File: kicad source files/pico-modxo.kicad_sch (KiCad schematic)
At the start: 9 parts, among them J1 XBOX_LPC, U1 Pico

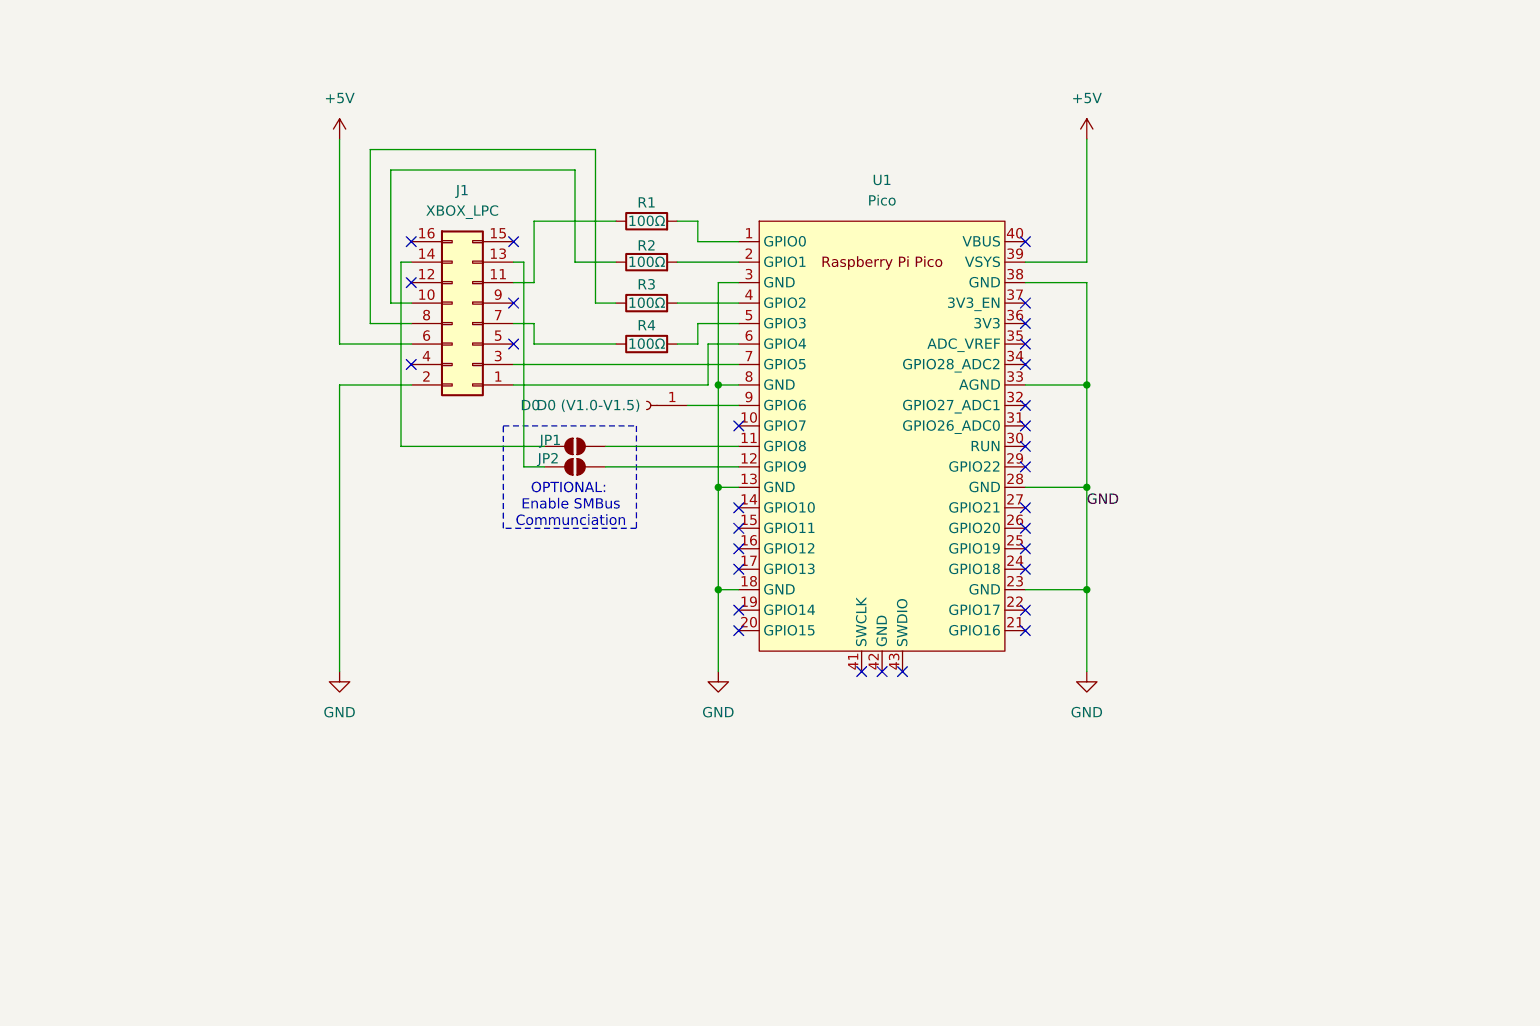
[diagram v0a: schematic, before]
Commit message: V2 Design
V2 Design based on EqUiNoX schematic 1.0 2024-07-29
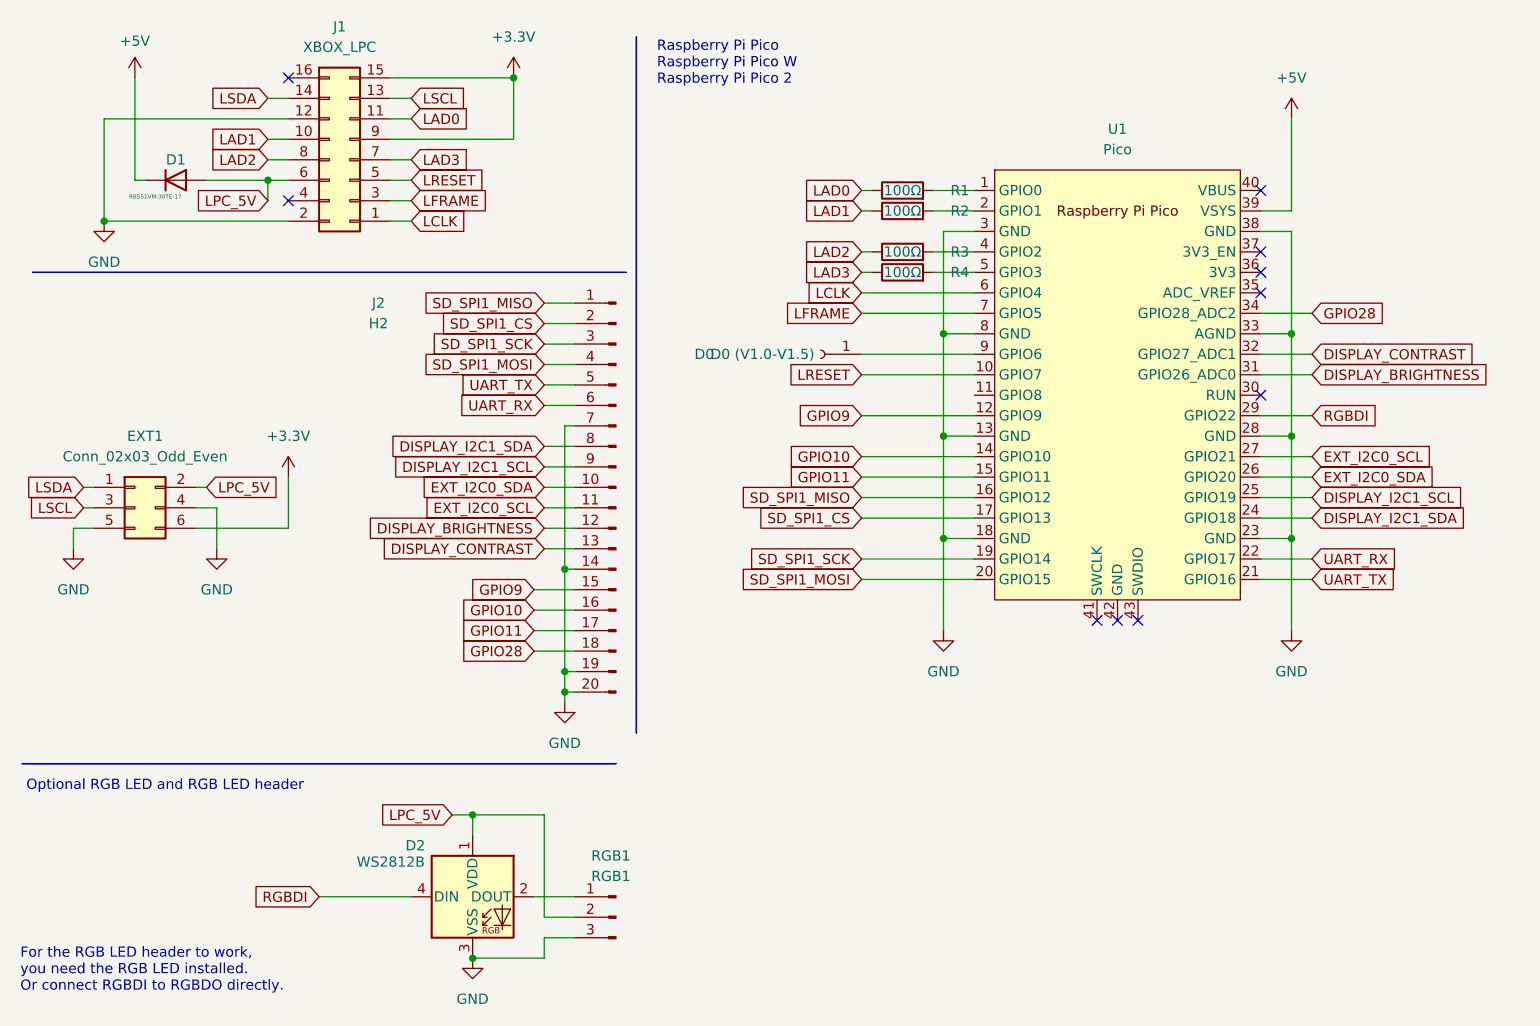
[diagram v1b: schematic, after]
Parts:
- removed JP1, JP2: SolderJumper_2_Open, Jumper:SolderJumper-2_P1.3mm_Open_RoundedPad1.0x1.5mm, symbol Jumper:SolderJumper_2_Open
- added D1: RB551VM-30TE-17, Diode_SMD:D_MELF-RM10_Universal_Handsoldering, symbol Device:D
- added D2: WS2812B, LED_SMD:LED_WS2812B_PLCC4_5.0x5.0mm_P3.2mm, symbol LED:WS2812B
- added EXT1: Conn_02x03_Odd_Even, Connector_PinHeader_2.54mm:PinHeader_2x03_P2.54mm_Vertical, symbol Connector_Generic:Conn_02x03_Odd_Even
- added J2: H2, Connector_Molex:Molex_SL_171971-0020_1x20_P2.54mm_Vertical, symbol Connector:Conn_01x20_Pin
- added RGB1: RGB1, Connector:FanPinHeader_1x03_P2.54mm_Vertical, symbol Connector:Conn_01x03_Pin
- J1: footprint XBOX_LPC:XBOX_LPC -> xbox_lpc:xbox_lpc
- R1, R2, R3, R4: footprint Resistor_THT:R_Axial_DIN0207_L6.3mm_D2.5mm_P7.62mm_Horizontal -> Resistors_Universal:Resistor_SMD+THTuniversal_1206_RM10_HandSoldering
- U1: footprint RPi_Pico:RPi_Pico_SMD_TH -> MCU_RaspberryPi_and_Boards:RPi_Pico_SMD_TH; symbol pico:Pico -> MCU_RaspberryPi_and_Boards:Pico
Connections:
- net +5V: now also D1.1 (K); no longer J1.6 (5V)
- net GND: now also J1.12 (GND), D2.3 (VSS), EXT1.4 (Pin_4), EXT1.5 (Pin_5), J2.14 (Pin_14), J2.19 (Pin_19), J2.20 (Pin_20), J2.7 (Pin_7), RGB1.3 (Pin_3)
- net LAD1: now reaches J1.10 (LAD1), R2.1
- net LAD3: now reaches J1.7 (LAD3), R4.1
- net LAD2: now reaches J1.8 (LAD2), R3.1
- net LSDA: now reaches J1.14 (SDA)
- net LSDA: now also EXT1.1 (Pin_1)
- net LAD0: now reaches J1.11 (LAD0), R1.1
- net LRESET: now reaches U1.10 (GPIO7)
- net LRESET: now also J1.5 (LRESET#)
- net GPIO9: now reaches U1.12 (GPIO9)
- net GPIO9: now also J2.15 (Pin_15)
- net GPIO10: now reaches U1.14 (GPIO10)
- net GPIO10: now also J2.16 (Pin_16)
- net GPIO11: now reaches U1.15 (GPIO11)
- net GPIO11: now also J2.17 (Pin_17)
- net SD_SPI1_MISO: now reaches U1.16 (GPIO12)
- net SD_SPI1_MISO: now also J2.1 (Pin_1)
- net SD_SPI1_CS: now reaches U1.17 (GPIO13)
- net SD_SPI1_CS: now also J2.2 (Pin_2)
- net SD_SPI1_SCK: now reaches U1.19 (GPIO14)
- net SD_SPI1_SCK: now also J2.3 (Pin_3)
- net SD_SPI1_MOSI: now reaches U1.20 (GPIO15)
- net SD_SPI1_MOSI: now also J2.4 (Pin_4)
- net UART_TX: now reaches U1.21 (GPIO16)
- net UART_TX: now also J2.5 (Pin_5)
- net UART_RX: now reaches U1.22 (GPIO17)
- net UART_RX: now also J2.6 (Pin_6)
- net DISPLAY_I2C1_SDA: now reaches U1.24 (GPIO18)
- net DISPLAY_I2C1_SDA: now also J2.8 (Pin_8)
- net DISPLAY_I2C1_SCL: now reaches U1.25 (GPIO19)
- net DISPLAY_I2C1_SCL: now also J2.9 (Pin_9)
- net EXT_I2C0_SDA: now reaches U1.26 (GPIO20)
- net EXT_I2C0_SDA: now also J2.10 (Pin_10)
- net EXT_I2C0_SCL: now reaches U1.27 (GPIO21)
- net EXT_I2C0_SCL: now also J2.11 (Pin_11)
- net RGBDI: now reaches U1.29 (GPIO22)
- net RGBDI: now also D2.4 (DIN)
- net DISPLAY_BRIGHTNESS: now reaches U1.31 (GPIO26_ADC0)
- net DISPLAY_BRIGHTNESS: now also J2.12 (Pin_12)
- net DISPLAY_CONTRAST: now reaches U1.32 (GPIO27_ADC1)
- net DISPLAY_CONTRAST: now also J2.13 (Pin_13)
- net GPIO28: now reaches U1.34 (GPIO28_ADC2)
- net GPIO28: now also J2.18 (Pin_18)
- net LCLK: now reaches J1.1 (LCLK), U1.6 (GPIO4)
- net LFRAME: now reaches J1.3 (LFRAME#), U1.7 (GPIO5)
- net LSCL: now reaches J1.13 (SCL)
- net LSCL: now also EXT1.3 (Pin_3)
- net +3.3V: now reaches J1.15 (3.3V)
- net +3.3V: now also J1.9 (3.3V), EXT1.6 (Pin_6)
- new net: D2.2 (DOUT), RGB1.1 (Pin_1)
- new net LPC_5V: D1.2 (A), D2.1 (VDD), EXT1.2 (Pin_2), J1.6 (5V), RGB1.2 (Pin_2)
- no-connect marks 31 -> 10
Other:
- note added: "Optional RGB LED and RGB LED header"
- note added: "Raspberry Pi Pico Raspberry Pi Pico W Raspberry Pi Pico 2"
- note removed: "Enable SMBus Communciation"
- note removed: "OPTIONAL:"
- company: (none) -> Version for future PrometheOS functionalities
- moved on the sheet: D0, J1, R1, R2, R3, R4, U1

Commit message: Move GND add GP8
added Gp8 connected to 3.3v
moved GND to bottom.
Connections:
- net +3.3V: now also U1.11 (GPIO8)
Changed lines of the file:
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@@
+	(wire
+		(pts
+			(xy 124.46 59.69) (xy 132.08 59.69)
+		)
+		(stroke
+			(width 0)
+			(type default)
+		)
+	)
 	(wire
 		(pts
@@
 					(unit 1)
 				)
+			)
+		)
+	)
+	(symbol
+		(lib_id "power:+3.3V")
+		(at 124.46 59.69 90)
+		(unit 1)
+		(exclude_from_sim no)
+		(in_bom yes)
+		(on_board yes)
+		(dnp no)
+		(fields_autoplaced yes)
+		(property "Reference" "#PWR012"
+			(at 128.27 59.69 0)
+			(effects
+				(font
+					(size 1.27 1.27)
+				)
+				(hide yes)
+			)
+		)
+		(property "Value" "+3.3V"
+			(at 120.65 59.6899 90)
+			(effects
+				(font
+					(size 1.27 1.27)
+				)
+				(justify left)
+			)
+		)
+		(property "Footprint" ""
+			(at 124.46 59.69 0)
+			(effects
+				(font
+					(size 1.27 1.27)
+				)
+				(hide yes)
+			)
+		)
+		(property "Datasheet" ""
+			(at 124.46 59.69 0)
+			(effects
+				(font
+					(size 1.27 1.27)
+				)
+				(hide yes)
+			)
+		)
+		(property "Description" "Power symbol creates a global label with name \"+3.3V\""
+			(at 124.46 59.69 0)
+			(effects
+				(font
+					(size 1.27 1.27)
+				)
+				(hide yes)
+			)
+		)
+		(pin "1"
+		)
+		(instances
+			(project "pico-modxo"
+				(path "/21d77f03-7f1f-46f6-89c7-87f98b707b4a"
+					(reference "#PWR012")
+					(unit 1)
+				)

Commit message: Pico ModXo V1.0
Release V1.0
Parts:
- D0: symbol Connector:Conn_01x01_Socket -> Connector:Conn_01x01_Female
- EXT1: value Conn_02x03_Odd_Even -> 2.54mm pin
- J2: value H2 -> 2.54mm pin; symbol Connector:Conn_01x20_Pin -> Connector:Conn_01x20_Male
- RGB1: value RGB1 -> 2.54mm pin; symbol Connector:Conn_01x03_Pin -> Connector:Conn_01x03_Male
- U1: value Pico -> Raspberry Pi Pico
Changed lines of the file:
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@@
 	(wire
 		(pts
+			(xy 130.81 27.94) (xy 130.81 59.69)
+		)
+		(stroke
+			(width 0)
+			(type default)
+		)
+	)
+	(wire
+		(pts
 			(xy 27.94 33.02) (xy 29.21 33.02)
 		)
@@
 	(wire
 		(pts
+			(xy 130.81 59.69) (xy 132.08 59.69)
+		)
+		(stroke
+			(width 0)
+			(type default)
+		)
+	)
+	(wire
+		(pts
 			(xy 167.64 36.83) (xy 171.45 36.83)
 		)
@@
 	(wire
 		(pts
-			(xy 171.45 36.83) (xy 171.45 25.4)
+			(xy 171.45 36.83) (xy 171.45 27.94)
 		)
 		(stroke
@@
 	(wire
 		(pts
-			(xy 124.46 59.69) (xy 132.08 59.69)
-		)
-		(stroke
-			(width 0)
-			(type default)
-		)
-	)
-	(wire
-		(pts
 			(xy 167.64 39.37) (xy 171.45 39.37)
 		)
@@
 			)
 		)
-		(property "Value" "Conn_02x03_Odd_Even"
+		(property "Value" "2.54mm pin"
 			(at 29.21 67.31 0)
 			(effects
@@
 		(dnp no)
 		(property "Reference" "R2"
-			(at 130.302 36.83 90)
+			(at 127.508 36.83 90)
 			(effects
 				(font
@@
 	(symbol
 		(lib_id "power:+5V")
-		(at 171.45 25.4 0)
+		(at 171.45 27.94 0)
 		(unit 1)
 		(exclude_from_sim no)
@@
 		(fields_autoplaced yes)
 		(property "Reference" "#PWR03"
-			(at 171.45 29.21 0)
+			(at 171.45 31.75 0)
 			(effects
 				(font
@@
 		)
 		(property "Value" "+5V"
-			(at 171.45 20.32 0)
+			(at 171.45 22.86 0)
 			(effects
 				(font
@@
 		)
 		(property "Footprint" ""
-			(at 171.45 25.4 0)
+			(at 171.45 27.94 0)
 			(effects
 				(font
@@
 		)
 		(property "Datasheet" ""
-			(at 171.45 25.4 0)
+			(at 171.45 27.94 0)
 			(effects
 				(font
@@
 		)
 		(property "Description" "Power symbol creates a global label with name \"+5V\""
-			(at 171.45 25.4 0)
+			(at 171.45 27.94 0)
 			(effects
 				(font
@@
 		(dnp no)
 		(property "Reference" "R4"
-			(at 130.302 44.45 90)
+			(at 127.508 44.45 90)
 			(effects
 				(font
@@
 		(dnp no)
 		(property "Reference" "R3"
-			(at 130.302 41.91 90)
+			(at 127.508 41.91 90)
 			(effects
 				(font
@@
 		(dnp no)
 		(property "Reference" "R1"
-			(at 130.302 34.29 90)
+			(at 127.508 34.29 90)
 			(effects
 				(font
@@
 	(symbol
 		(lib_id "power:+3.3V")
-		(at 124.46 59.69 90)
+		(at 130.81 27.94 0)
 		(unit 1)
 		(exclude_from_sim no)
@@
 		(on_board yes)
 		(dnp no)
-		(fields_autoplaced yes)
 		(property "Reference" "#PWR012"
-			(at 128.27 59.69 0)
+			(at 130.81 31.75 0)
 			(effects
 				(font
@@
 		)
 		(property "Value" "+3.3V"
-			(at 120.65 59.6899 90)
+			(at 127.762 23.114 0)
 			(effects
 				(font
@@
 		)
 		(property "Footprint" ""
-			(at 124.46 59.69 0)
+			(at 130.81 27.94 0)
 			(effects
 				(font
@@
 		)
 		(property "Datasheet" ""
-			(at 124.46 59.69 0)
+			(at 130.81 27.94 0)
 			(effects
 				(font
@@
 		)
 		(property "Description" "Power symbol creates a global label with name \"+3.3V\""
-			(at 124.46 59.69 0)
+			(at 130.81 27.94 0)
 			(effects
 				(font
@@
 	)
 	(symbol
-		(lib_id "Connector:Conn_01x03_Pin")
+		(lib_id "Connector:Conn_01x03_Male")
 		(at 87.63 124.46 0)
 		(mirror y)
@@
 			)
 		)
-		(property "Value" "RGB1"
+		(property "Value" "2.54mm pin"
 			(at 86.995 119.38 0)
 			(effects
@@
 			)
 		)
-		(property "Description" "Generic connector, single row, 01x03, script generated"
+		(property "Description" "Generic connector, single row, 01x03, script generated (kicad-library-utils/schlib/autogen/connector/)"
 			(at 87.63 124.46 0)
 			(effects
@@
 	)
 	(symbol
-		(lib_id "Connector:Conn_01x01_Socket")
+		(lib_id "Connector:Conn_01x01_Female")
 		(at 113.03 54.61 0)
 		(mirror y)
@@
 			)
 		)
-		(property "Description" "Generic connector, single row, 01x01, script generated"
+		(property "Description" "Generic connector, single row, 01x01, script generated (kicad-library-utils/schlib/autogen/connector/)"
 			(at 113.03 54.61 0)
 			(effects
@@
 	)
 	(symbol
-		(lib_id "Connector:Conn_01x20_Pin")
+		(lib_id "Connector:Conn_01x20_Male")
 		(at 87.63 71.12 0)
 		(mirror y)
@@
 			)
 		)
-		(property "Value" "H2"
+		(property "Value" "2.54mm pin"
 			(at 58.166 50.8 0)
 			(effects
@@
 			)
 		)
-		(property "Description" "Generic connector, single row, 01x20, script generated"
+		(property "Description" "Generic connector, single row, 01x20, script generated (kicad-library-utils/schlib/autogen/connector/)"
 			(at 87.63 71.12 0)
 			(effects
@@
 			)
 		)
-		(property "Value" "Pico"
+		(property "Value" "Raspberry Pi Pico"
 			(at 149.86 29.21 0)
 			(effects
